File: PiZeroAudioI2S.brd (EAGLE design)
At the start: 65.1 x 30.2 mm, 52 parts, among them CON1 RPI-ZERO, J1 GROVE, J2 2X2HEADER, J3 2X1-LOCKING, J4 4X1-LOCKING, Q1 DMG2305UX, U1 TXB0104PWR, U2 LSM6DS33, U4 DMMT5401, U5 TPA3144D2PWPR

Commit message: Performed layout
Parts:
- removed R16, R17, R18: 33K, adafruit:R0603
- removed R19: 10R, adafruit:R0603
- added C27, C30: 1uF, rcl:C0603
- added C28, C31: 1nF, rcl:C0603
- added C29: 220nF, rcl:C0603
- added C3: 0.1uF, rcl:C0603
- added C32, C6: 100nF, rcl:C0603
- added C33: 100UF, adafruit:CT3528
- added C4: 10uF, adafruit:CT3528
- added C7: 2.2nF, rcl:C0603
- added C8: 2.2uF, rcl:C0603
- added R10: 39K, adafruit:R0603
- added R5, R6: 470, adafruit:R0603
- added R7, R9: 10K, adafruit:R0603
- added R8: 47K, adafruit:R0603
- added U3: PCM5101A, HappyBrackets:TSSOP20-0.65-6.5X4.4MM
- C10: value 100nF -> 0.1uF
- C11: value 100uF -> 10uF
- C12: value 220nF -> 0.1uF
- C13: value 1uF -> 10uF; device rcl:C0603 -> adafruit:CT3528
- C14: value 1nF -> 0.1uF
- C15: value 1nF -> 10uF; device rcl:C0603 -> adafruit:CT3528
- C16, C22: value 220nF -> 1nF
- C17: value 220nF -> 100nF
- C18: value 1uF -> 100uF; device rcl:C0603 -> adafruit:CT3528
- C19, C24: value 1nF -> 220nF
- C23: value 1uF -> 220nF
- C25: value 100nF -> 1uF
- C26: value 100UF -> 1nF; device adafruit:CT3528 -> rcl:C0603
- C5: value 100nF -> 2.2nF
- C9: value 1nF -> 2.2uF
- R11: value 10K -> 56K
- R12: value 47K -> 33K
- R13: value 10K -> 33K
- R14: value 39K -> 33K
- R15: value 56K -> 10R
- moved C11 42.8 mm to (-31.7, 23.0), turned to 180 degrees
- moved C15 31.4 mm to (-37.7, 23.0), turned to 180 degrees
- moved C5 31.2 mm to (-40.3, 15.4), turned to 270 degrees
- moved C14 30.1 mm to (-39.3, 19.9), turned to 180 degrees
- moved C10 27.8 mm to (-36.1, 19.9), turned to 180 degrees
- moved C9 26.0 mm to (-31.0, 11.1), turned to 180 degrees
- moved C18 25.4 mm to (-70.5, 4.95), turned to 90 degrees
- moved C12 24.8 mm to (-33.9, 9.60), turned to 90 degrees
- moved R11 15.3 mm to (-42.9, 11.6), turned to 0 degrees
- moved C25 14.9 mm to (-46.0, 11.6), turned to 0 degrees
- moved C23 14.2 mm to (-58.9, 9.98)
- moved R13 14.1 mm to (-42.9, 15.9), turned to 180 degrees
- moved R15 12.4 mm to (-49.5, 18.4), turned to 180 degrees
- moved R12 12.2 mm to (-42.9, 17.9), turned to 0 degrees
- moved SH1 10.9 mm to (-25.5, 18.1)
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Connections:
- removed net PWM-L: CON1.35
- removed net PWM-R: CON1.12
- new net N$1: R5.1, U3.7
- new net N$11: R6.1, U3.6
- new net N$12: C10.1, C11.-, U3.18
- new net N$2: C8.1, U3.5
- new net N$3: C9.1, U3.4
- new net N$4: C9.2, U3.2
- new net PCM-CLK: CON1.12, U3.13
- new net PCM_DOUT: CON1.40, U3.14
- new net PCM_FS: CON1.35, U3.15
- net +3V3: now also C14.2, C15.+, C6.1, U3.17, U3.20; no longer C5.1
- net +5V: now also C16.1, C17.1, C18.+, C31.1, C32.1, C33.+, R15.2; no longer C10.1, C11.+, C24.1, C25.1, C26.+, C9.1, R19.2
- net /MUTE: now also R7.1; no longer R11.1
- net AGND: now also C12.1, C13.-, C16.2, C17.2, C18.-, C21.2, C22.1, C26.2, C27.2, C28.1, C3.1, C30.2, C31.2, C32.2, C33.-, C4.-, C5.2, C7.2, C8.2, R10.2, R8.2, R9.2, U3.3, U3.9; no longer C10.2, C11.-, C13.2, C14.2, C15.1, C18.2, C19.2, C21.1, C23.2, C24.2, C26.-, C9.2, R13.2, R14.2, R16.2
- net AN3V3: now also C12.2, C13.+, C3.2, C4.+, U3.1, U3.8
- net AUDIO-LEFT: now also C7.1, R6.2
- net AUDIO-RIGHT: now also C5.1, R5.2
- net GND: now also C10.2, C11.+, C14.1, C15.-, C6.2, U3.10, U3.11, U3.16, U3.19; no longer C5.2
- net L+: now also C21.1; no longer C14.1
- net L-: now also C22.2; no longer C15.2
- net N$10: now also C29.2; no longer C22.2
- net N$13: now also C24.2; no longer C17.2
- net N$16: now also C23.2; no longer C16.2
- net N$17: now also C19.2; no longer C12.2
- net N$18: now also C19.1; no longer C12.1
- net N$19: now also C23.1; no longer C16.1
- net N$20: now also C24.1; no longer C17.1
- net N$21: now also C29.1; no longer C22.1
- net N$22: now also R9.1; no longer R13.1
- net N$23: now also R12.1, R13.2; no longer R16.1, R17.2
- net N$24: now also R13.1, R14.2; no longer R17.1, R18.2
- net N$25: now also R10.1, R11.2; no longer R14.1, R15.2
- net N$26: now also C25.1, R11.1, R14.1; no longer C18.1, R15.1, R18.1
- net N$27: now also R8.1; no longer R12.1
- net N$5: now also R7.2; no longer R11.2
- net N$7: now also C20.1; no longer C13.1
- net N$8: now also C27.1; no longer C20.1
- net N$9: now also C30.1, R15.1; no longer C23.1, R19.1
- net R+: now also C28.2; no longer C21.2
- net R-: now also C26.1; no longer C19.1
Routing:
- net +3V3: track 146.1 -> 67.7 mm, vias 3 -> 1
- net AGND: track 260.3 -> 199.6 mm, vias 14 -> 12
- net GND: track 159.2 -> 137.8 mm
- net N$26: track 28.5 -> 7.40 mm
- net PWM-R: track 20.0 -> 0.00 mm
- net N$24: track 22.8 -> 6.30 mm, vias 2 -> 0
- net GPIO21-OUT: track 13.6 -> 0.00 mm
- net N$25: track 14.2 -> 0.79 mm
- net PWM-L: track 13.1 -> 0.00 mm, vias 1 -> 0
- net PCM_FS: track 0.00 -> 12.2 mm
- net GPI022-OUT: track 11.9 -> 0.00 mm
- net GPIO21: track 9.94 -> 0.00 mm
- net GPIO23-OUT: track 9.04 -> 0.00 mm
- net GPIO25: track 8.03 -> 0.00 mm
- net GPIO25-OUT: track 7.61 -> 0.01 mm
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
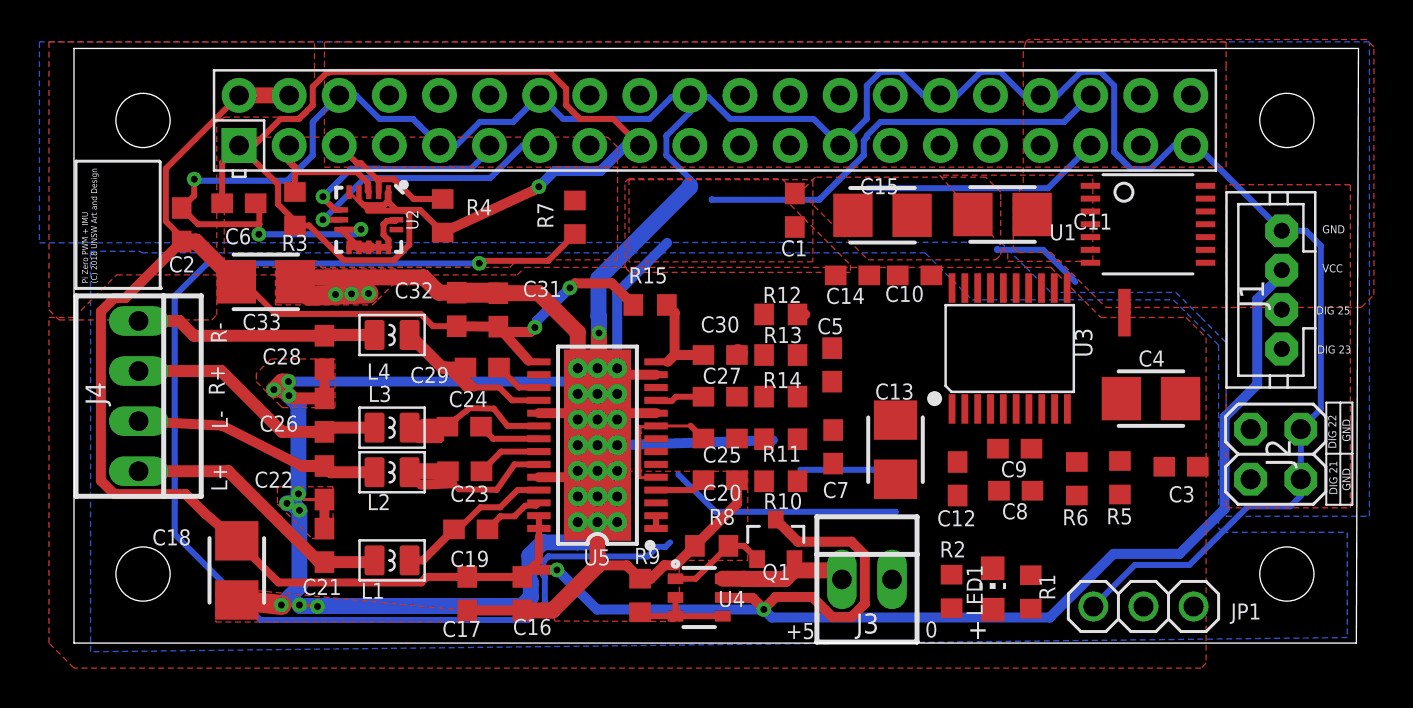
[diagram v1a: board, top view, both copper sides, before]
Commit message: Changed capacitor footprints
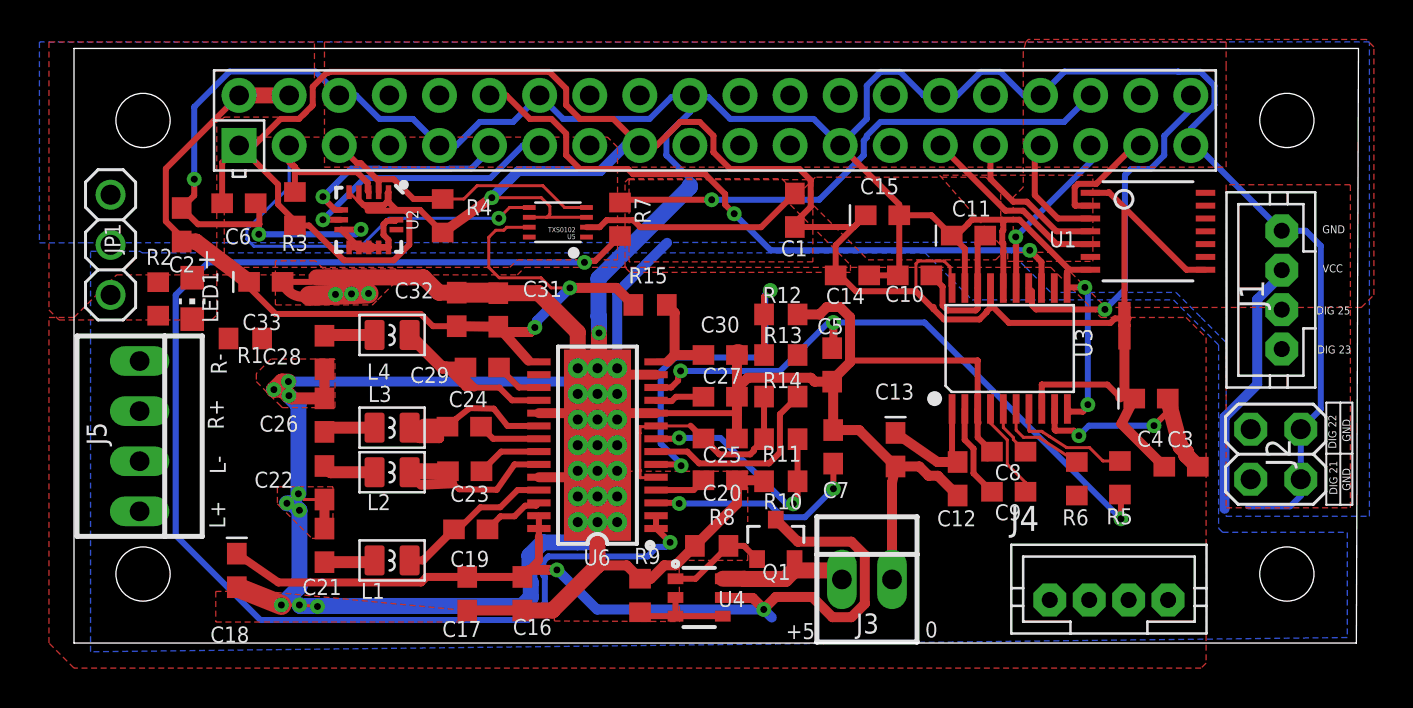
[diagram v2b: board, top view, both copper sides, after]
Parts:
- added J5: 4X1-LOCKING, HappyBrackets:22-23-2041
- added U6: TPA3144D2PWPR, HappyBrackets:HTSSOP28
- C11, C13, C15, C18, C33, C4: device adafruit:CT3528 -> HappyBrackets:0603-POLAR
- J4: value 4X1-LOCKING -> GROVE; device HappyBrackets:22-23-2041 -> HappyBrackets:JST-PH4
- U5: value TPA3144D2PWPR -> TXS0102; device HappyBrackets:HTSSOP28 -> adafruit:VFSOP-8
- moved JP1 55.5 mm to (-76.9, 21.5), turned to 270 degrees
- moved J4 50.3 mm to (-26.3, 3.45), turned to 0 degrees
- moved LED1 43.2 mm to (-72.7, 18.7), turned to 180 degrees
- moved R2 42.9 mm to (-74.5, 18.7)
- moved R1 41.8 mm to (-70.1, 16.7), turned to 0 degrees
- moved U5 11.5 mm to (-54.2, 22.6)
- moved R7 2.29 mm to (-51.1, 22.8)
- moved C9 2.21 mm to (-31.3, 8.94)
- moved C11 2.03 mm to (-33.4, 21.9)
- moved C8 2.01 mm to (-31.3, 11.0)
- moved SH1 0.66 mm to (-25.5, 17.4)
- moved U1 0.36 mm to (-24.3, 22.1)
- turned C3 to 180 degrees
- turned C4 to 180 degrees
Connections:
- new net SCL-OUT: J4.1, U5.P$1
- new net SDA-OUT: J4.2, U5.P$8
- net +3V3: now also U5.P$3, U5.P$6
- net +5V: now also J4.3, U5.P$7, U6.15, U6.16, U6.27, U6.28; no longer U5.15, U5.16, U5.27, U5.28
- net AGND: now also U6.10, U6.13, U6.19, U6.24, U6.GND@10, U6.GND@11, U6.GND@12, U6.GND@13, U6.GND@14, U6.GND@15, U6.GND@16, U6.GND@17, U6.GND@18, U6.GND@19, U6.GND@20, U6.GND@21, U6.GND@22, U6.GND@23, U6.GND@24, U6.GND@25, U6.GND@26, U6.GND@27, U6.GND@28, U6.GND@29, U6.GND@30, U6.GND@PAD; no longer U5.10, U5.13, U5.19, U5.24, U5.GND@10, U5.GND@11, U5.GND@12, U5.GND@13, U5.GND@14, U5.GND@15, U5.GND@16, U5.GND@17, U5.GND@18, U5.GND@19, U5.GND@20, U5.GND@21, U5.GND@22, U5.GND@23, U5.GND@24, U5.GND@25, U5.GND@26, U5.GND@27, U5.GND@28, U5.GND@29, U5.GND@30, U5.GND@PAD
- net AUDIO-LEFT: now also U6.3; no longer U5.3
- net AUDIO-RIGHT: now also U6.12; no longer U5.12
- net GND: now also J4.4, U5.P$2
- net L+: now also J5.4; no longer J4.4
- net L-: now also J5.3; no longer J4.3
- net N$10: now also U6.17; no longer U5.17
- net N$13: now also U6.21; no longer U5.21
- net N$16: now also U6.22; no longer U5.22
- net N$17: now also U6.26; no longer U5.26
- net N$18: now also U6.25; no longer U5.25
- net N$19: now also U6.23; no longer U5.23
- net N$20: now also U6.20; no longer U5.20
- net N$21: now also U6.18; no longer U5.18
- net N$23: now also U6.6; no longer U5.6
- net N$24: now also U6.7; no longer U5.7
- net N$25: now also U6.8; no longer U5.8
- net N$26: now also U6.5, U6.9; no longer U5.5, U5.9
- net N$5: now also U6.1, U6.2; no longer U5.1, U5.2
- net N$7: now also U6.4; no longer U5.4
- net N$8: now also U6.11; no longer U5.11
- net N$9: now also U6.14; no longer U5.14
- net R+: now also J5.1; no longer J4.1
- net R-: now also J5.2; no longer J4.2
- net SCL: now also U5.P$4
- net SDA: now also U5.P$5
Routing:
- net +3V3: track 67.7 -> 126.1 mm
- net AGND: track 199.6 -> 255.2 mm, vias 12 -> 14
- net GND: track 137.8 -> 178.7 mm, vias 4 -> 6
- net +5V: track 150.3 -> 111.0 mm
- net PCM-CLK: track 0.00 -> 33.8 mm, vias 0 -> 2
- net AUDIO-RIGHT: track 0.00 -> 31.9 mm, vias 0 -> 3
- net SDA: track 7.44 -> 28.4 mm, vias 0 -> 1
- net AN3V3: track 0.00 -> 20.2 mm
- net PCM_DOUT: track 0.00 -> 18.0 mm, vias 0 -> 1
- net L+: track 13.9 -> 2.58 mm
- net AUDIO-LEFT: track 0.00 -> 11.2 mm, vias 0 -> 2
- net N$25: track 0.79 -> 11.7 mm, vias 0 -> 2
- net R-: track 13.3 -> 2.63 mm
- net L-: track 12.6 -> 2.67 mm
- net R+: track 12.3 -> 2.56 mm
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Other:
- board text removed: "Pi Zero PWM + IMU (C) 2018 UNSW Art and Design"

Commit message: Completed route
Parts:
- moved R2 0.15 mm to (-74.6, 18.7), turned to 270 degrees
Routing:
- net SCL-OUT: track 0.00 -> 84.2 mm, vias 0 -> 1
- net SDA-OUT: track 0.00 -> 55.0 mm, vias 0 -> 1
- net +5V: track 111.0 -> 154.2 mm, vias 4 -> 5
- net GND: track 178.7 -> 200.1 mm, vias 6 -> 7
- net +3V3: track 126.1 -> 143.9 mm
- net AGND: track 255.2 -> 270.2 mm, vias 14 -> 17
- net AUDIO-LEFT: track 11.2 -> 25.9 mm, vias 2 -> 3
- net N$24: track 9.96 -> 24.6 mm
- net GPIO21-OUT: track 0.00 -> 13.4 mm
- net AN3V3: track 20.2 -> 33.1 mm
- net GPI022-OUT: track 0.00 -> 11.8 mm
- net L+: track 2.58 -> 13.0 mm
- net R+: track 2.56 -> 12.6 mm
- net R-: track 2.63 -> 12.6 mm
- net L-: track 2.67 -> 12.1 mm
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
